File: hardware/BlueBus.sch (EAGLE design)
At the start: 128 parts, among them Q1 NMOSFET-BSS138K, Q2 PMOSFET-DMP1045UQ, Q3 NMOSFET-BSS138K, X1 CRYSTAL-12MHZ

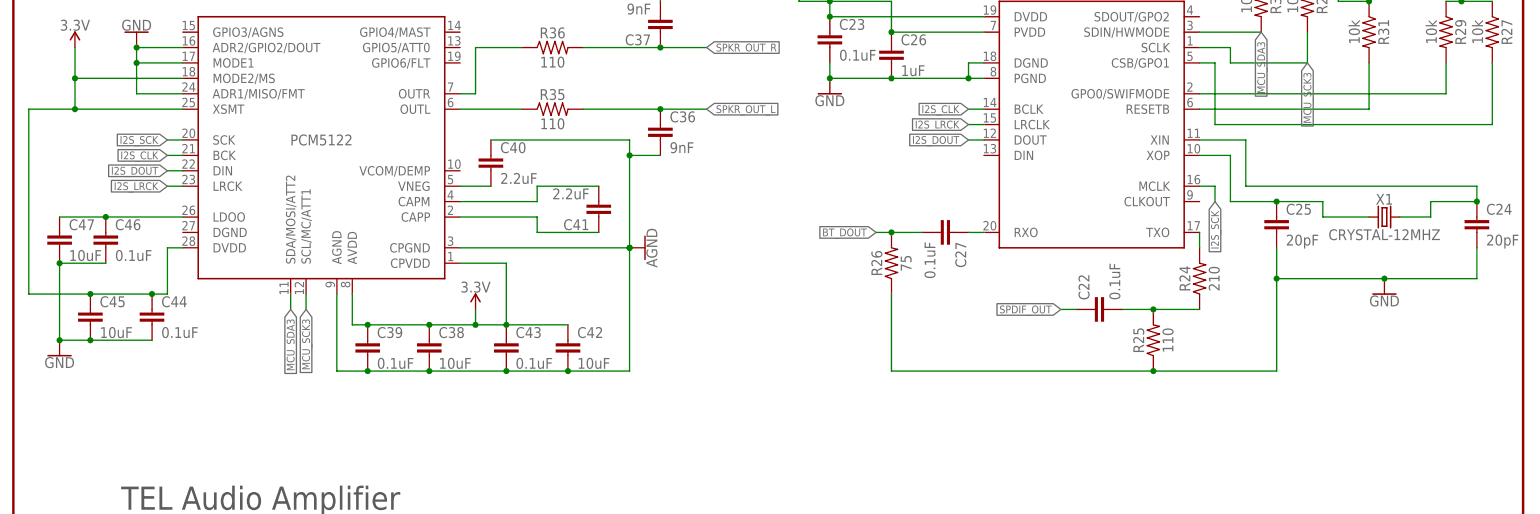
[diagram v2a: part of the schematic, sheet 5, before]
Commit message: [IMP] hardware: Production V1 * Add Fiducials * Fix bugs with PCM5122 DGND being floating and VCOM not being tied to AGND * Adjust routing so that all traces intersect at 90 degree angles on different layers * Adjust traces to not follow the same track on different sides of the board * Add additional ground stiches * Improve placement of decoupling caps for superior ground returns
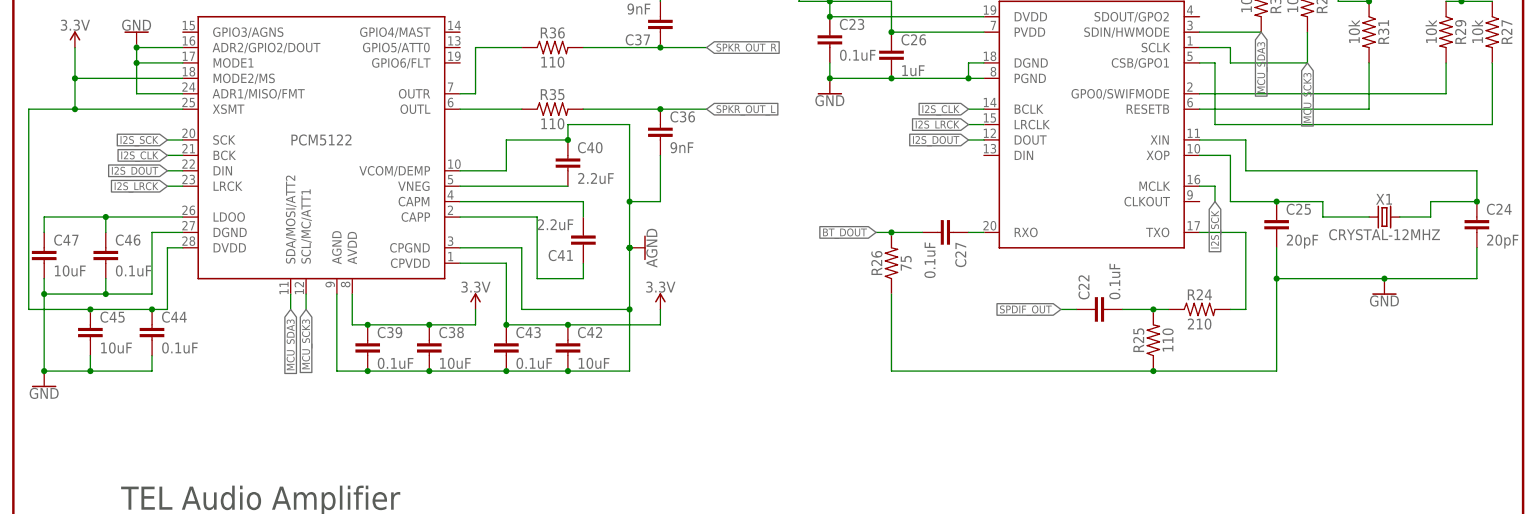
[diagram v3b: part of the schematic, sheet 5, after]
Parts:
- added FID1, FID2, FID3, FID4, FID5: FIDUCIAL_0.5MM, MF_Aesthetics:FIDUCIAL_0.5MM
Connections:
- new net 12V_VIN: D1.A, PWR_IN.2
- new net BT_URX_RES: BC127.UART_RX, R21.2
- new net RAW_3.3V: C6.1, F2.IN, XC6210.VOUT
- new net VIN_DIODE: D1.C, F1.OUT
- net 3.3V: no longer C6.1, F2.IN, XC6210.VOUT
- net AGND: now also PCM5122.VCOM/DEMP
- net BT_URX: no longer BC127.UART_RX, R21.2
- net GND: now also PCM5122.DGND
- net VIN: no longer D1.A, D1.C, F1.OUT, PWR_IN.2
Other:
- moved on the sheet: C2, C40, C41, C44, C45, C46, C47, D2, F2, R21, R24, R5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

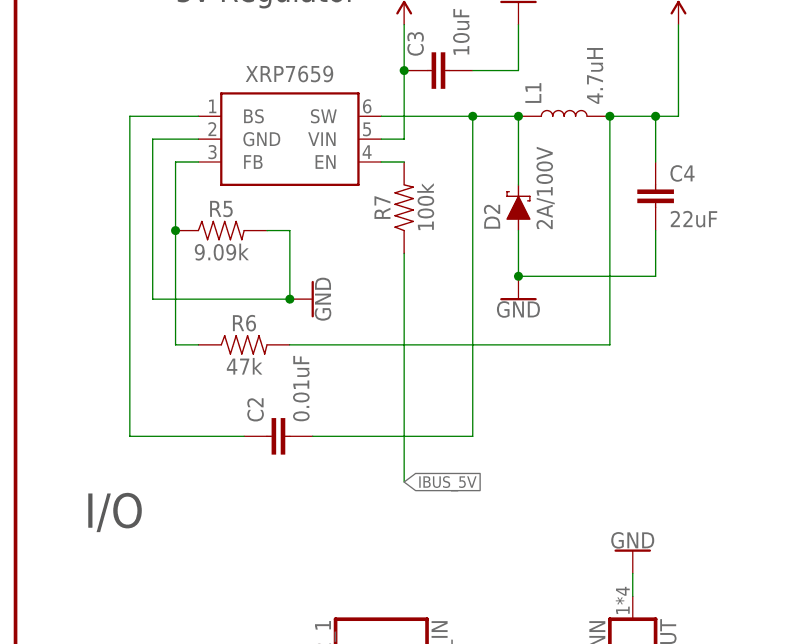
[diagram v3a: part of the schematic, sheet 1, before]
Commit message: [IMP] hardware: Production V1 * Fix issue with silkscreen names * Add ground VIA
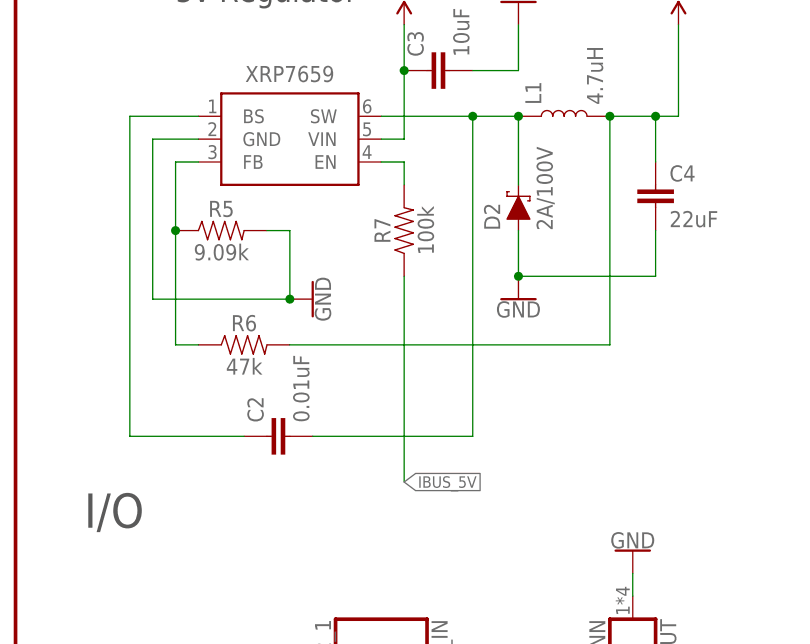
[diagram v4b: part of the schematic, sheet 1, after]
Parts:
- R28, R30: value 10k -> 4.7k; device Passives:10KOHM -> Passives:4.7KOHM
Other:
- moved on the sheet: R7
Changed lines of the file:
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@@
 <part name="R8" library="Passives" deviceset="4.7KOHM" device="" value="4.7k"/>
 <part name="R31" library="Passives" deviceset="10KOHM" device="" value="10k"/>
-<part name="R28" library="Passives" deviceset="10KOHM" device="" value="10k"/>
+<part name="R28" library="Passives" deviceset="4.7KOHM" device="" value="4.7k"/>
 <part name="R27" library="Passives" deviceset="10KOHM" device="" value="10k"/>
-<part name="R30" library="Passives" deviceset="10KOHM" device="" value="10k"/>
+<part name="R30" library="Passives" deviceset="4.7KOHM" device="" value="4.7k"/>
 <part name="GND26" library="SparkFun-PowerSymbols" library_urn="urn:adsk.eagle:library:530" deviceset="GND" device=""/>
 <part name="R25" library="Passives" deviceset="110OHM" device="" value="110"/>
@@
 <attribute name="DRAWING_NAME" x="152.654" y="17.78" size="2.7432" layer="94" font="vector"/>
 </instance>
-<instance part="R7" gate="G$1" x="43.18" y="147.32" smashed="yes" rot="R90">
-<attribute name="NAME" x="41.656" y="147.32" size="1.778" layer="95" font="vector" rot="R90" align="bottom-center"/>
-<attribute name="VALUE" x="44.704" y="147.32" size="1.778" layer="96" font="vector" rot="R90" align="top-center"/>
+<instance part="R7" gate="G$1" x="43.18" y="144.78" smashed="yes" rot="R90">
+<attribute name="NAME" x="41.656" y="144.78" size="1.778" layer="95" font="vector" rot="R90" align="bottom-center"/>
+<attribute name="VALUE" x="44.704" y="144.78" size="1.778" layer="96" font="vector" rot="R90" align="top-center"/>
 </instance>
 <instance part="L1" gate="G$1" x="60.96" y="157.48" smashed="yes" rot="R90">
@@
 <pinref part="R7" gate="G$1" pin="2"/>
 <pinref part="XRP7659" gate="G$1" pin="EN"/>
-<wire x1="43.18" y1="152.4" x2="40.64" y2="152.4" width="0.1524" layer="91"/>
+<wire x1="40.64" y1="152.4" x2="43.18" y2="152.4" width="0.1524" layer="91"/>
+<wire x1="43.18" y1="152.4" x2="43.18" y2="149.86" width="0.1524" layer="91"/>
 </segment>
 </net>
@@
 <segment>
 <pinref part="R7" gate="G$1" pin="1"/>
-<wire x1="43.18" y1="142.24" x2="43.18" y2="116.84" width="0.1524" layer="91"/>
+<wire x1="43.18" y1="139.7" x2="43.18" y2="116.84" width="0.1524" layer="91"/>
 <label x="43.18" y="116.84" size="1.27" layer="95" xref="yes"/>
 </segment>
@@
 <segment>
 <pinref part="GND18" gate="1" pin="GND"/>
-<wire x1="81.28" y1="20.32" x2="81.28" y2="17.78" width="0.1524" layer="91"/>
 <pinref part="C20" gate="G$1" pin="2"/>
 <wire x1="66.04" y1="40.64" x2="66.04" y2="38.1" width="0.1524" layer="91"/>
 <wire x1="66.04" y1="38.1" x2="81.28" y2="38.1" width="0.1524" layer="91"/>
 <wire x1="81.28" y1="38.1" x2="81.28" y2="35.56" width="0.1524" layer="91"/>
-<wire x1="81.28" y1="35.56" x2="81.28" y2="20.32" width="0.1524" layer="91"/>
+<wire x1="81.28" y1="35.56" x2="81.28" y2="17.78" width="0.1524" layer="91"/>
 <pinref part="TMUX154E" gate="G$1" pin="EN"/>
-<wire x1="50.8" y1="20.32" x2="81.28" y2="20.32" width="0.1524" layer="91"/>
-<junction x="81.28" y="20.32"/>
+<junction x="81.28" y="17.78"/>
 <pinref part="TMUX154E" gate="G$1" pin="GND"/>
 <wire x1="60.96" y1="35.56" x2="81.28" y2="35.56" width="0.1524" layer="91"/>
 <junction x="81.28" y="35.56"/>
-</segment>
-</net>
+<wire x1="50.8" y1="20.32" x2="50.8" y2="17.78" width="0.1524" layer="91"/>
+<wire x1="50.8" y1="17.78" x2="81.28" y2="17.78" width="0.1524" layer="91"/>
+</segment>
+</net>

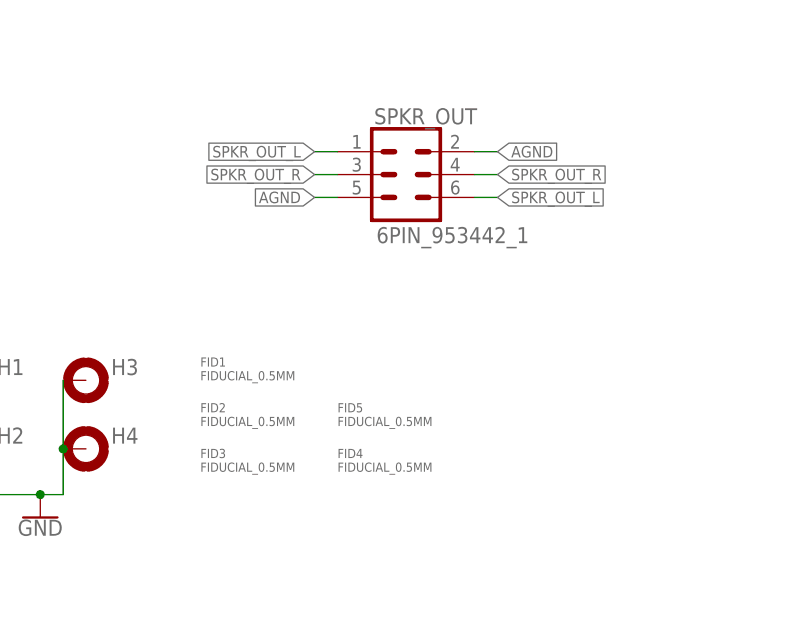
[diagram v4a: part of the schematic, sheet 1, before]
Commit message: [IMP] hardware: V 1.1 * Reroute 3.3v rail under the PIC24 to prevent ground returns on the second layer from having to take a longer route * Bring 5v rail to top layer for a short run in order to open the ground return path (to the left of the PIC24) * Leave pin 3 of the SPKR_OUT connector floating to prevent audio channel grounding on certain models * Add space between the edge of the analog audio ground plane end and the R/L channel traces * VIA stitch layers around the ground "bridge" (right above the BlueBus name on the Silkscreen) * Increase GND bridge to 1mm from 0.75mm * Increase BC127 pad size to allow more paste to fill the castellations * Bring RC filter for BC127 closer to power pin
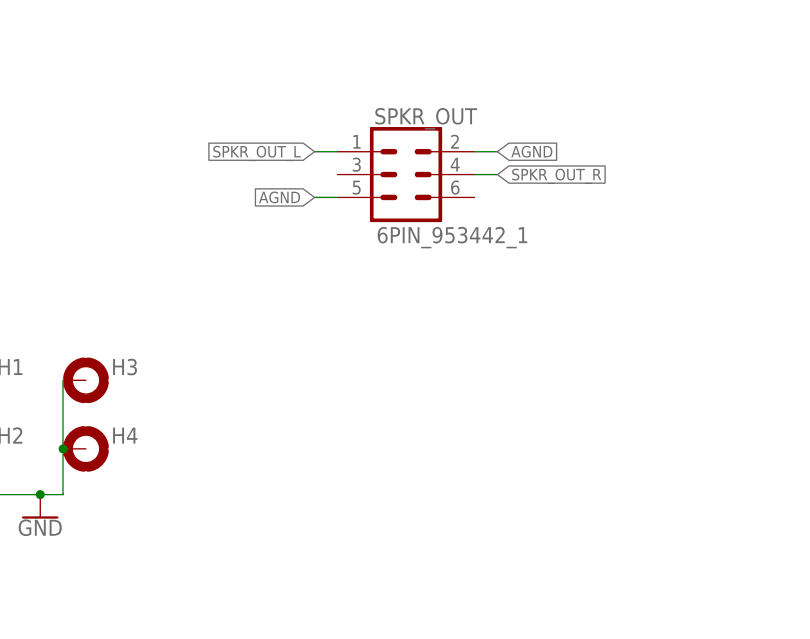
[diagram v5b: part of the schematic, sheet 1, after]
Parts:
- removed FID1, FID2, FID3, FID4, FID5: FIDUCIAL_0.5MM, MF_Aesthetics:FIDUCIAL_0.5MM
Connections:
- net SPKR_OUT_L: no longer SPKR_OUT.6
- net SPKR_OUT_R: no longer SPKR_OUT.3
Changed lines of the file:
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@@
 <part name="SUPPLY4" library="SparkFun-PowerSymbols" library_urn="urn:adsk.eagle:library:530" deviceset="5V" device=""/>
 <part name="GND31" library="SparkFun-PowerSymbols" library_urn="urn:adsk.eagle:library:530" deviceset="GND" device=""/>
-<part name="FID1" library="MF_Aesthetics" deviceset="FIDUCIAL" device="_0.5MM"/>
-<part name="FID2" library="MF_Aesthetics" deviceset="FIDUCIAL" device="_0.5MM"/>
-<part name="FID3" library="MF_Aesthetics" deviceset="FIDUCIAL" device="_0.5MM"/>
-<part name="FID4" library="MF_Aesthetics" deviceset="FIDUCIAL" device="_0.5MM"/>
-<part name="FID5" library="MF_Aesthetics" deviceset="FIDUCIAL" device="_0.5MM"/>
 <part name="SUPPLY2" library="SparkFun-PowerSymbols" library_urn="urn:adsk.eagle:library:530" deviceset="3.3V" device=""/>
 </parts>
@@
 <attribute name="VALUE" x="33.274" y="137.16" size="1.778" layer="96" rot="R90" align="top-center"/>
 </instance>
-<instance part="FID1" gate="G$1" x="43.18" y="33.02" smashed="yes">
-<attribute name="VALUE" x="43.18" y="31.496" size="1.016" layer="96" font="vector" rot="MR180"/>
-<attribute name="NAME" x="43.18" y="33.02" size="1.016" layer="95" font="vector" rot="MR180"/>
-</instance>
-<instance part="FID2" gate="G$1" x="43.18" y="27.94" smashed="yes">
-<attribute name="VALUE" x="43.18" y="26.416" size="1.016" layer="96" font="vector" rot="MR180"/>
-<attribute name="NAME" x="43.18" y="27.94" size="1.016" layer="95" font="vector" rot="MR180"/>
-</instance>
-<instance part="FID3" gate="G$1" x="43.18" y="22.86" smashed="yes">
-<attribute name="VALUE" x="43.18" y="21.336" size="1.016" layer="96" font="vector" rot="MR180"/>
-<attribute name="NAME" x="43.18" y="22.86" size="1.016" layer="95" font="vector" rot="MR180"/>
-</instance>
-<instance part="FID4" gate="G$1" x="58.42" y="22.86" smashed="yes">
-<attribute name="VALUE" x="58.42" y="21.336" size="1.016" layer="96" font="vector" rot="MR180"/>
-<attribute name="NAME" x="58.42" y="22.86" size="1.016" layer="95" font="vector" rot="MR180"/>
-</instance>
-<instance part="FID5" gate="G$1" x="58.42" y="27.94" smashed="yes">
-<attribute name="VALUE" x="58.42" y="26.416" size="1.016" layer="96" font="vector" rot="MR180"/>
-<attribute name="NAME" x="58.42" y="27.94" size="1.016" layer="95" font="vector" rot="MR180"/>
-</instance>
 </instances>
 <busses>
@@
 <net name="SPKR_OUT_R" class="0">
 <segment>
-<pinref part="SPKR_OUT" gate="G$1" pin="3"/>
-<wire x1="58.42" y1="53.34" x2="55.88" y2="53.34" width="0.1524" layer="91"/>
-<label x="55.88" y="53.34" size="1.27" layer="95" rot="R180" xref="yes"/>
-</segment>
-<segment>
 <pinref part="SPKR_OUT" gate="G$1" pin="4"/>
 <wire x1="73.66" y1="53.34" x2="76.2" y2="53.34" width="0.1524" layer="91"/>
@@
 <net name="SPKR_OUT_L" class="0">
 <segment>
-<pinref part="SPKR_OUT" gate="G$1" pin="6"/>
-<wire x1="73.66" y1="50.8" x2="76.2" y2="50.8" width="0.1524" layer="91"/>
-<label x="76.2" y="50.8" size="1.27" layer="95" xref="yes"/>
-</segment>
-<segment>
 <pinref part="SPKR_OUT" gate="G$1" pin="1"/>
